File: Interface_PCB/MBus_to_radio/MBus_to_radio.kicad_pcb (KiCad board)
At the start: 2 copper layers, 26.5 x 60.5 mm, 21 parts, among them Q1 BC847, Q2 BC857, U1 AP63205WU-7, X1 TB003-500-P02BE

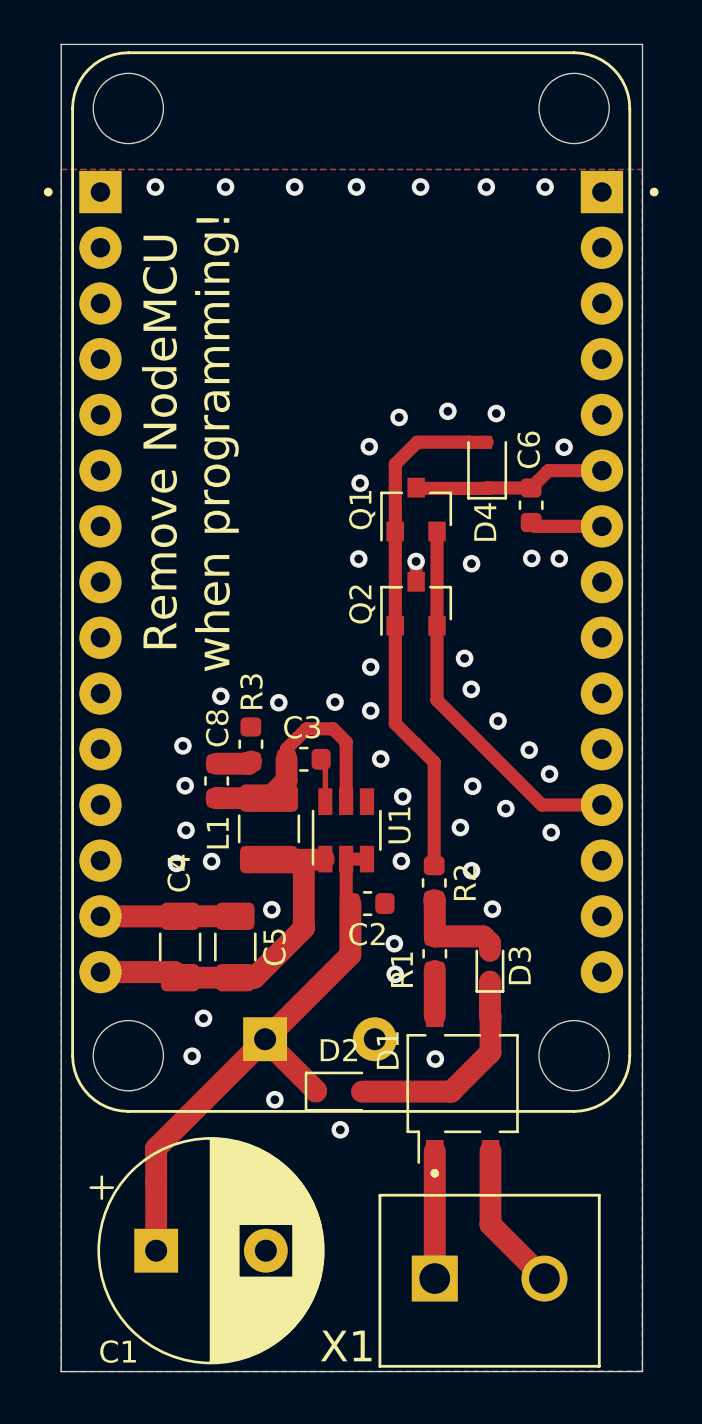
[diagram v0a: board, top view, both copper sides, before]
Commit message: update PCB V2 to version that was produced
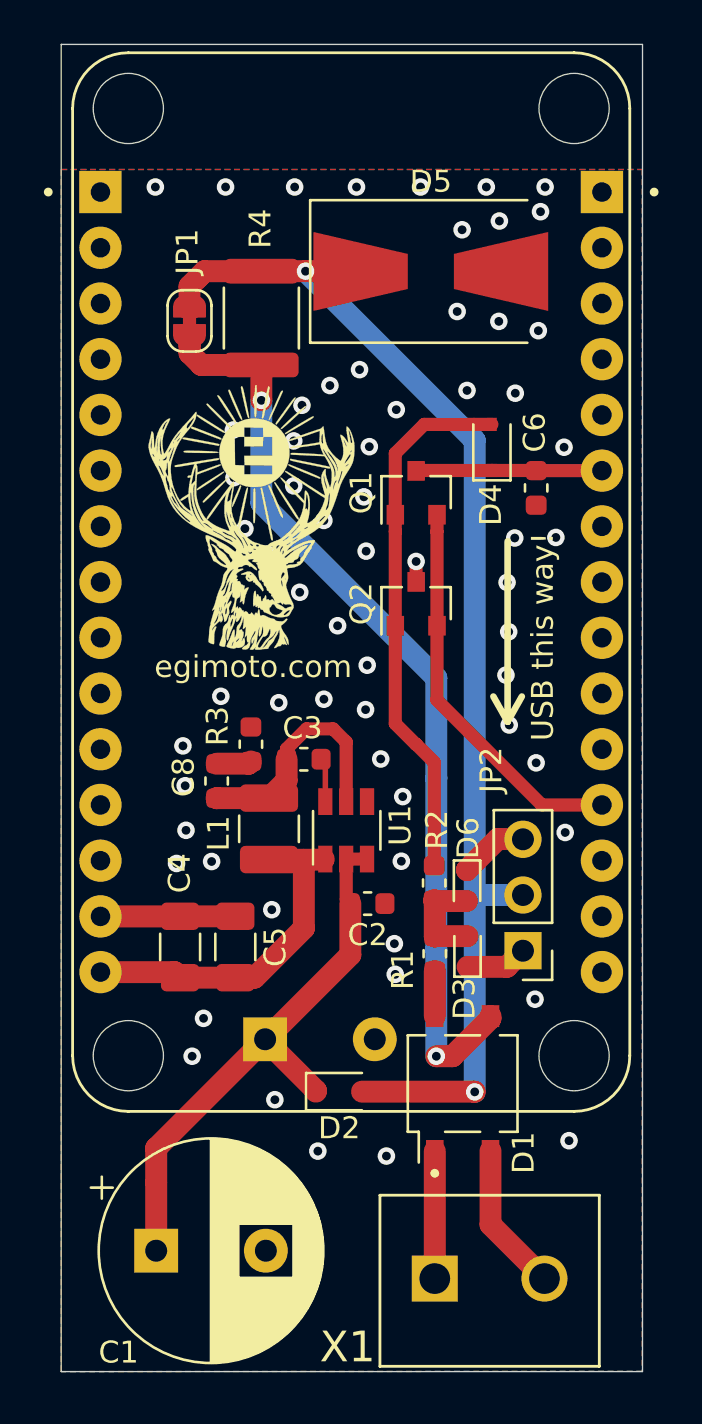
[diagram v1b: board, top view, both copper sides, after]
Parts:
- added D5: SZ1SMB5936BT3G, Diode_SMD:D_SMB-SMC_Universal_Handsoldering, F.Cu at (112.8, 65.8)
- added D6: SZMM5Z24VT5GF, Diode_SMD:D_SOD-523, F.Cu at (114.5, 93.8)
- added G***: LOGO, Grafics:egimoto_hirsch, F.Cu at (104.7, 77.0)
- added JP1: SolderJumper_2_Bridged, Jumper:SolderJumper-2_P1.3mm_Bridged_RoundedPad1.0x1.5mm, F.Cu at (101.8, 68.1)
- added JP2: Select Smartmeter type, Connector_PinHeader_2.54mm:PinHeader_1x03_P2.54mm_Vertical, F.Cu at (117.0, 96.8)
- added R4: 1R, Resistor_SMD:R_1812_4532Metric, F.Cu at (105.1, 68.0)
- C2, C3: value 100n -> 100n 50V
- C4, C5: value 22u -> 22u 10V
- C6: value 100n -> 100n 16V
- C8: value 1n -> 1n 50V
- moved D3 1.22 mm to (114.5, 96.8)
- moved D4 0.84 mm to (115.6, 73.9)
- moved C6 0.82 mm to (117.7, 75.7)
- moved Q1 0.76 mm to (112.2, 75.9)
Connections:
- A1 pad J2_15: Net-(A1-PadJ2_15) -> +3V3
- A1 pad J2_6: Net-(A1-PadJ2_15) -> +3V3
- D1 pad 3: VBUS -> Net-(D1-Pad3)
- D3 pad 1: VBUS -> Net-(D3-Pad1)
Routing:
- net VBUS: track 9.84 -> 57.0 mm, vias 0 -> 2
- net Net-(D1-Pad3): track 0.00 -> 42.9 mm, vias 0 -> 2
- net GND: track 12.4 -> 9.14 mm, vias 50 -> 64
- net Net-(D6-Pad1): track 0.00 -> 3.16 mm
- net Net-(D3-Pad1): track 0.00 -> 2.83 mm
- net Net-(D4-Pad2): track 23.7 -> 24.5 mm
- net M-Bus_Data_out: track 17.2 -> 17.9 mm
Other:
- board text added: "EVN Interface V2 Tobias Ecker 11-2022"
- board text added: "No:"
- board text added: "SW: Matthias Preymann"
- board text added: "USB this way!"
- board text added: "egimoto.com"
- board text removed: "EVN Kaifa Interface V2 Tobias Ecker 11-2022"
